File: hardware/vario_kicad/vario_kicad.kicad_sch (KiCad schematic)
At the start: 8 parts, among them U1 STM32L071CBTx, U2 BME280

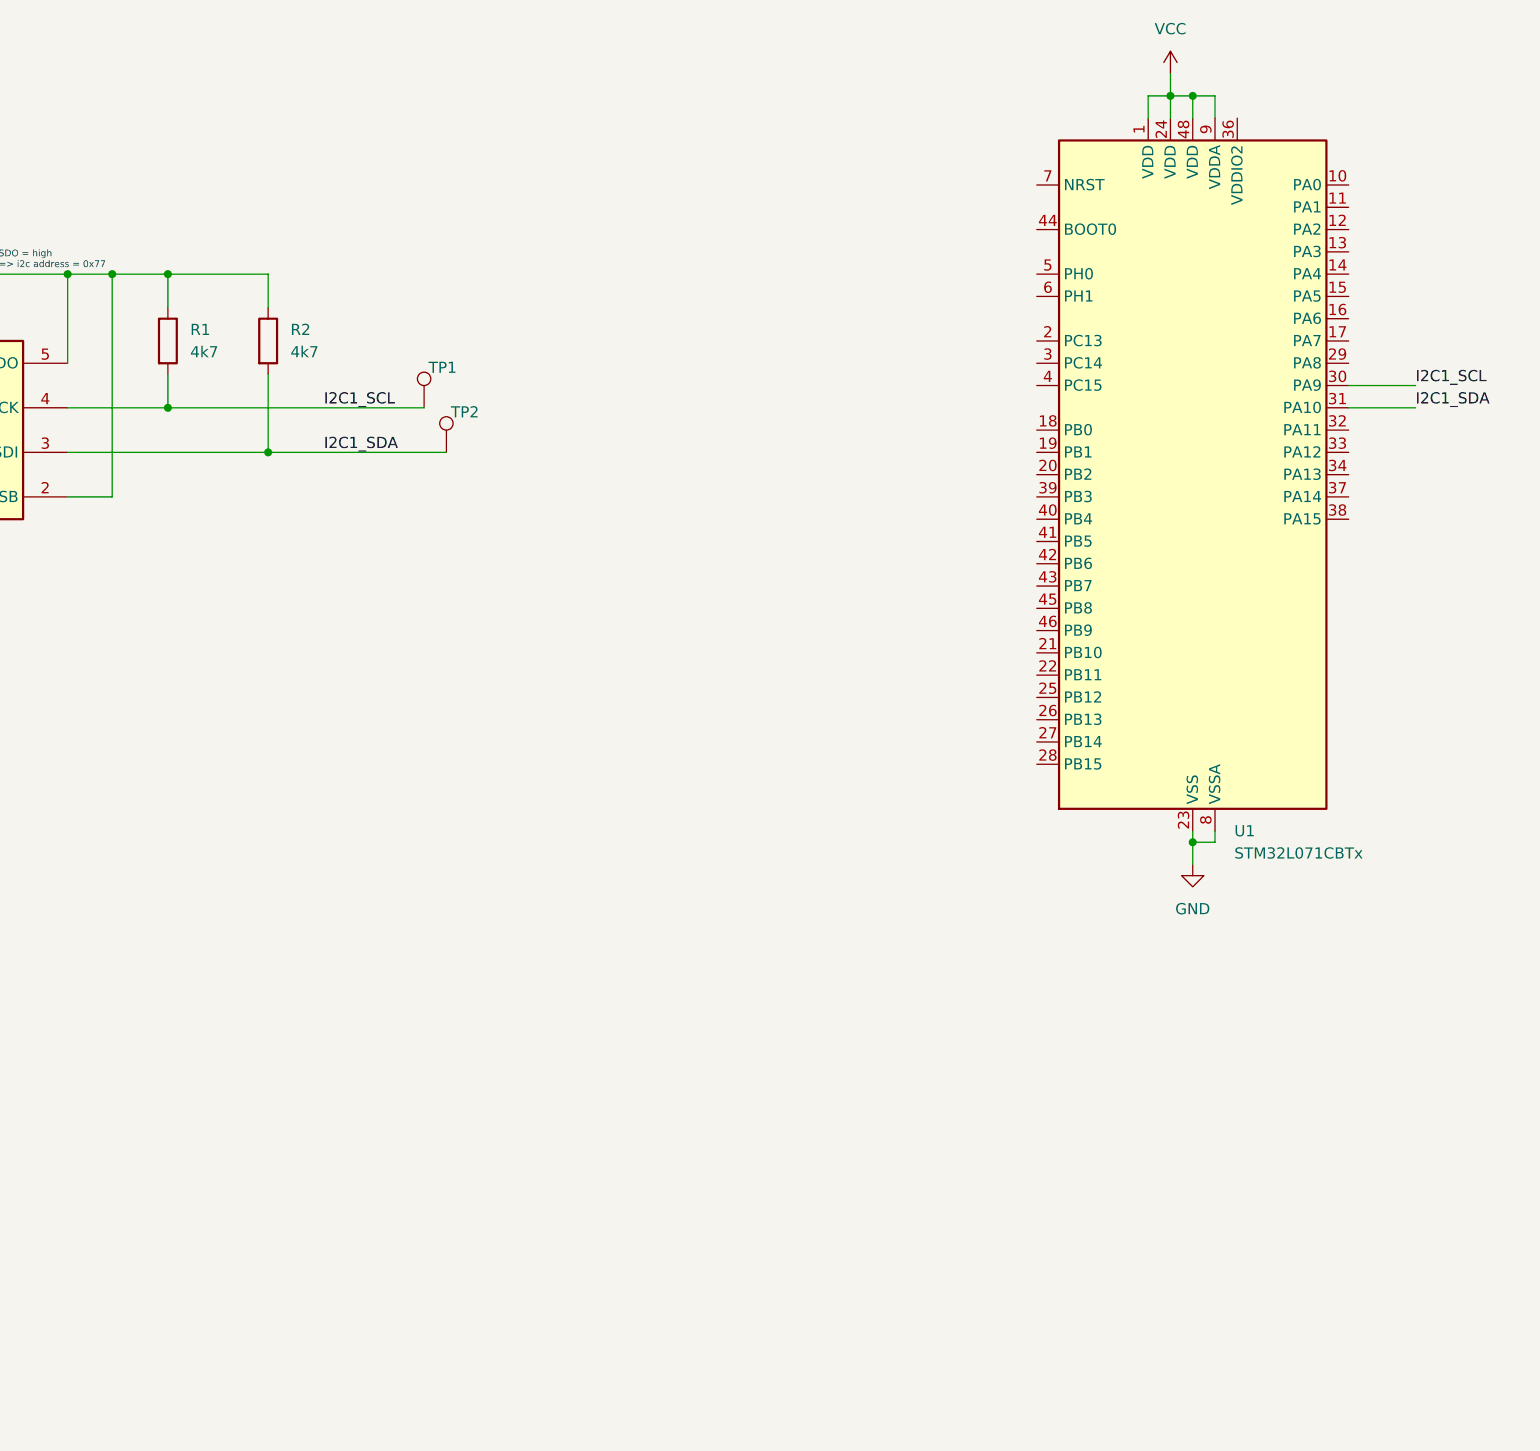
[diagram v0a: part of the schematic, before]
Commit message: add external memory chip
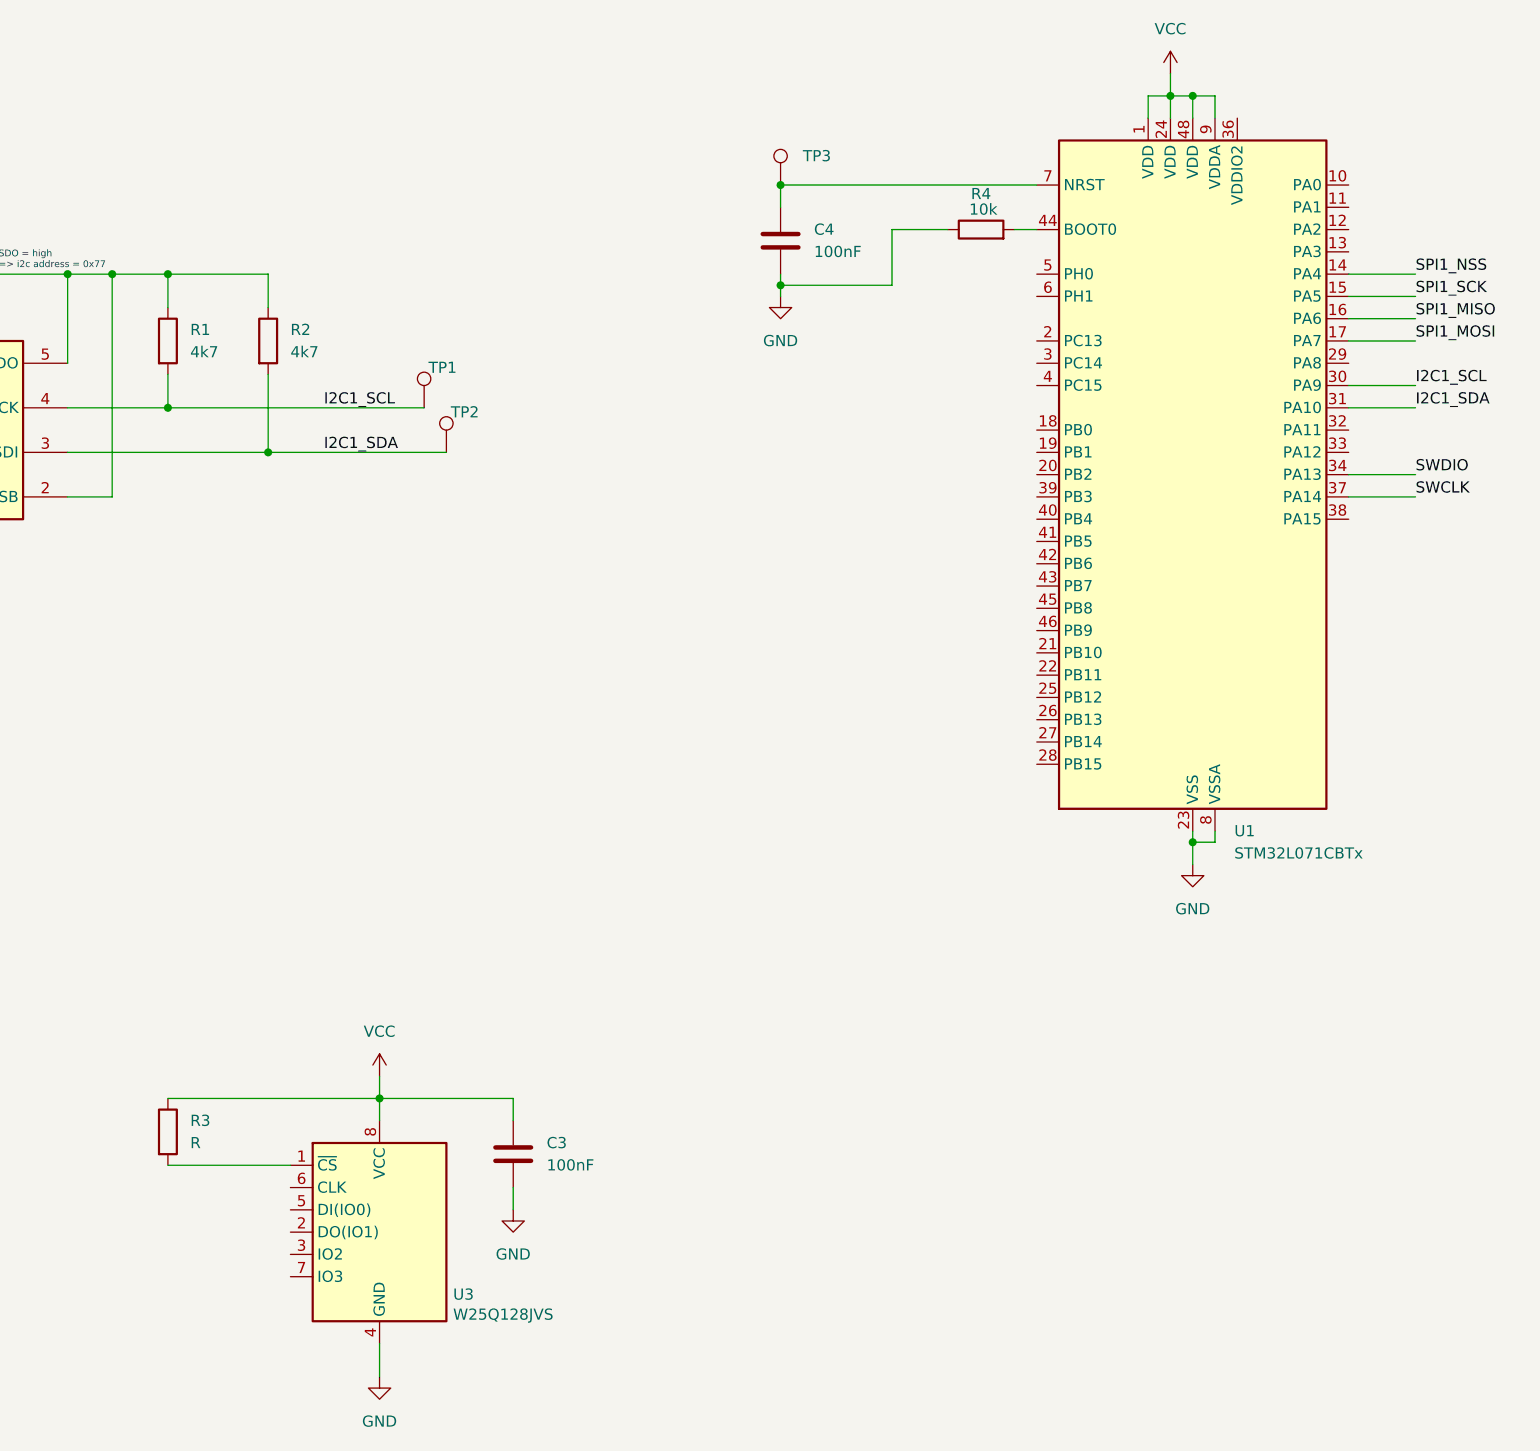
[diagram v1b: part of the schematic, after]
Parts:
- added C3, C4: 100nF, symbol Device:C
- added R3: R, symbol Device:R
- added R4: 10k, symbol Device:R
- added TP3: ~, symbol Connector:TestPoint
- added U3: W25Q128JVS, Package_SO:SOIC-8_5.23x5.23mm_P1.27mm, symbol Memory_Flash:W25Q128JVS
- TP1, TP2: value (none) -> ~
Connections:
- net GND: now also C3.2, C4.2, R4.1, U3.4 (GND)
- net VCC: now also C3.1, R3.1, U3.8 (VCC)
- net SPI1_NSS: now reaches U1.14 (PA4)
- net SPI1_SCK: now reaches U1.15 (PA5)
- net SPI1_MISO: now reaches U1.16 (PA6)
- net SPI1_MOSI: now reaches U1.17 (PA7)
- net SWDIO: now reaches U1.34 (PA13)
- net SWCLK: now reaches U1.37 (PA14)
- net at U1.44 (BOOT0): now also R4.2
- net at U1.7 (NRST): now also C4.1, TP3.1
- new net: R3.2, U3.1 (~{CS})

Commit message: update hw
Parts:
- added D1, D2, D3: LED, symbol Device:LED
- added R10, R11: 10k, symbol Device:R
- added R12, R13, R14: 330R, symbol Device:R
- added R5, R6, R7, R8, R9: 0R, symbol Device:R
- added TP4: ~, symbol Connector:TestPoint
- R3: value R -> 10k
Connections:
- net GND: now also R12.2, R13.2, R14.2
- net SPI1_MISO: now also R7.1
- net SPI1_MOSI: now also R6.1
- net SPI1_NSS: now also R8.1
- net SPI1_SCK: now also R5.1
- net VCC: now also R10.1, R11.1
- net BOOT0: now reaches R4.2, U1.44 (BOOT0)
- net BOOT0: now also TP4.1
- net NRST: now reaches C4.1, TP3.1, U1.7 (NRST)
- net at R3.2, U3.1 (~{CS}): now also R8.2, R9.2
- net at U3.2 (DO(IO1)): now also R7.2
- net MEM_WP: now reaches U3.3 (WP(IO2))
- net MEM_WP: now also R10.2
- net at U3.5 (DI(IO0)): now also R6.2
- net at U3.6 (CLK): now also R5.2
- net MEM_HOLD: now reaches U3.7 (IO3)
- net MEM_HOLD: now also R11.2
- net RED_LED: now reaches U1.10 (PA0)
- net RED_LED: now also D1.2 (A)
- net GREEN_LED: now reaches U1.11 (PA1)
- net GREEN_LED: now also D2.2 (A)
- net BLUE_LED: now reaches U1.12 (PA2)
- net BLUE_LED: now also D3.2 (A)
- new net: D2.1 (K), R13.1
- new net: D3.1 (K), R14.1
- new net: D1.1 (K), R12.1
- new net MEM_CS_ALT: R9.1
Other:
- moved on the sheet: C1, C2, C3, C4, R1, R2, R3, TP1, TP2, TP3, U2, U3

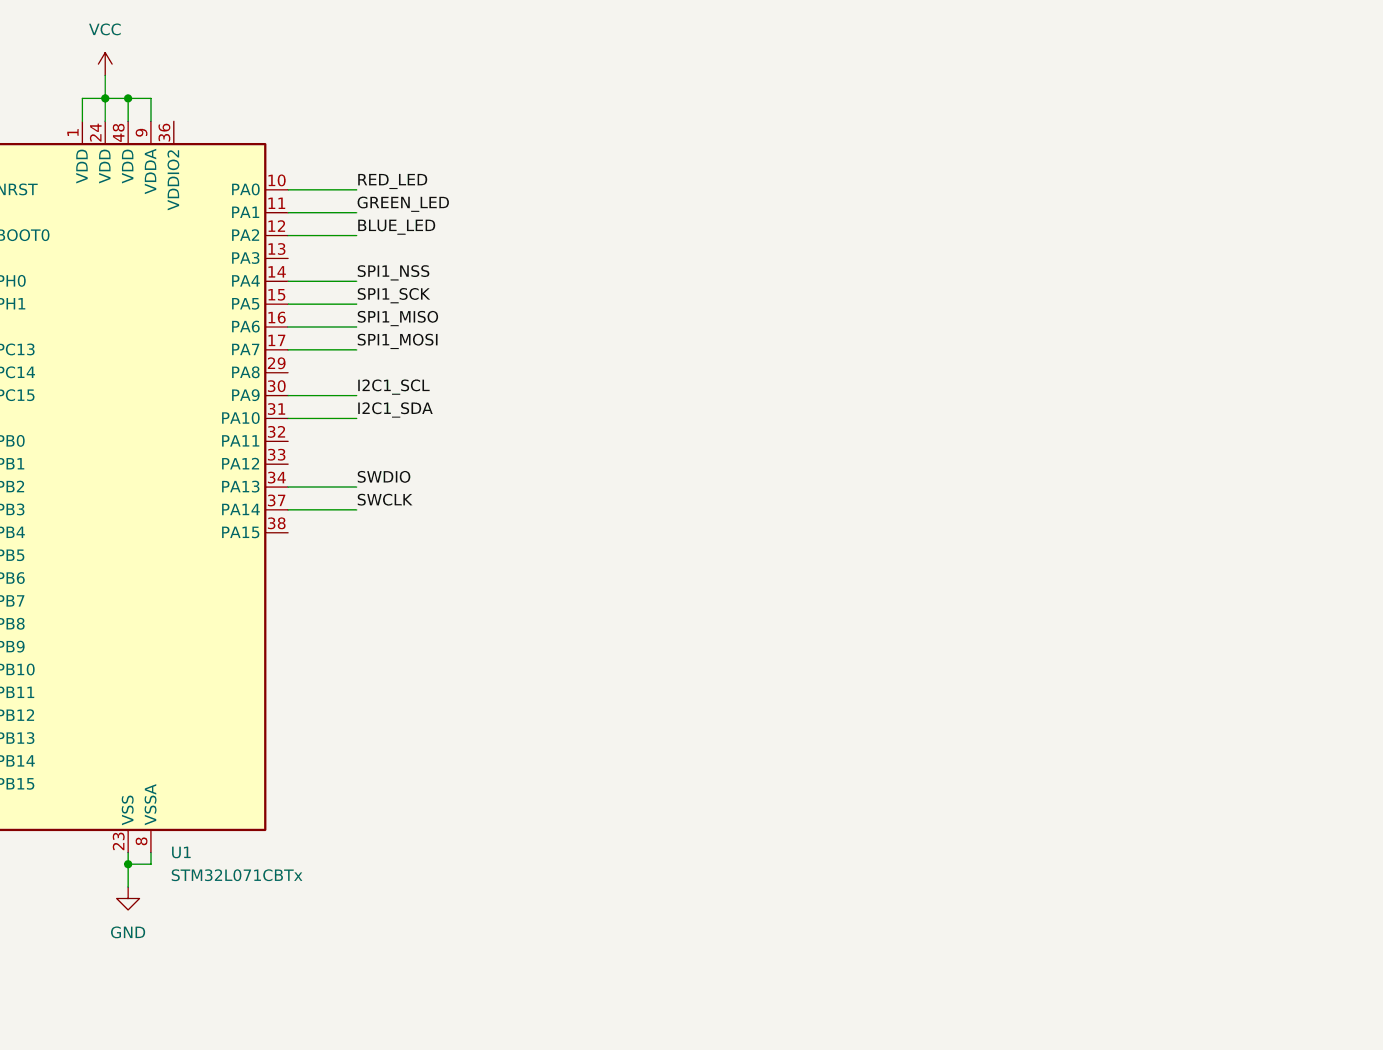
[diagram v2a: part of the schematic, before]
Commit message: update to stm32l072 processor for usb
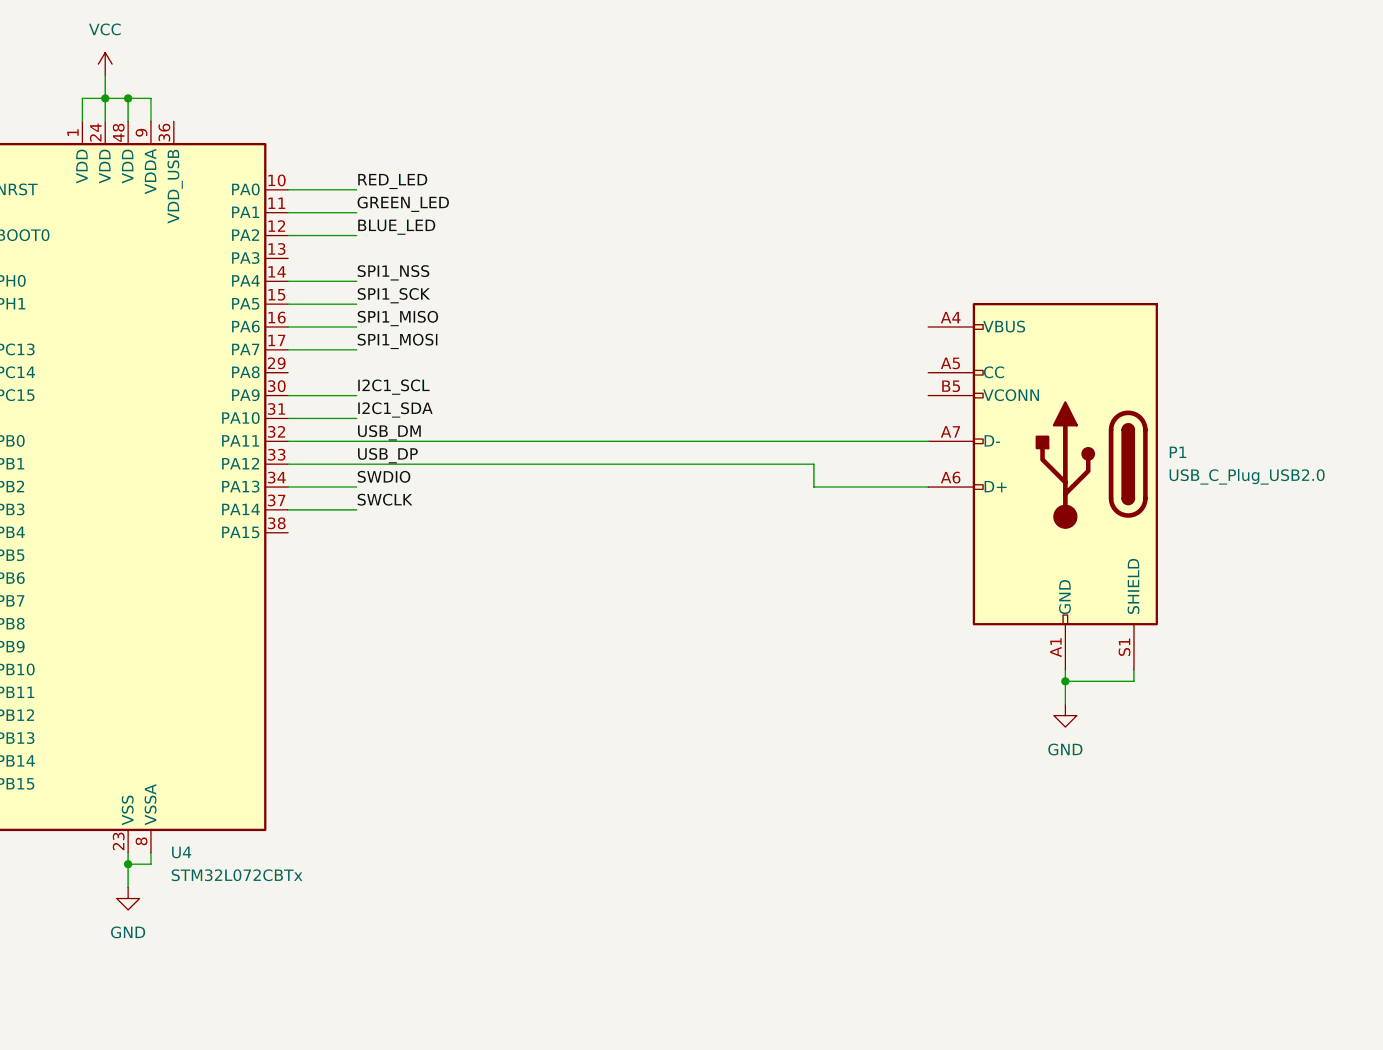
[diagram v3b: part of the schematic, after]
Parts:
- removed U1: STM32L071CBTx, Package_QFP:LQFP-48_7x7mm_P0.5mm, symbol MCU_ST_STM32L0:STM32L071CBTx
- added P1: USB_C_Plug_USB2.0, symbol Connector:USB_C_Plug_USB2.0
- added U4: STM32L072CBTx, Package_QFP:LQFP-48_7x7mm_P0.5mm, symbol MCU_ST_STM32L0:STM32L072CBTx
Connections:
- net BLUE_LED: now also U4.12 (PA2)
- net BOOT0: now also U4.44 (BOOT0)
- net GND: now also P1.A1 (GND), P1.A12 (GND), P1.B1 (GND), P1.B12 (GND), P1.S1 (SHIELD), U4.23 (VSS), U4.35 (VSS), U4.47 (VSS), U4.8 (VSSA)
- net GREEN_LED: now also U4.11 (PA1)
- net I2C1_SCL: now also U4.30 (PA9)
- net I2C1_SDA: now also U4.31 (PA10)
- net NRST: now also U4.7 (NRST)
- net RED_LED: now also U4.10 (PA0)
- net SPI1_MISO: now also U4.16 (PA6)
- net SPI1_MOSI: now also U4.17 (PA7)
- net SPI1_NSS: now also U4.14 (PA4)
- net SPI1_SCK: now also U4.15 (PA5)
- net SWCLK: now also U4.37 (PA14)
- net SWDIO: now also U4.34 (PA13)
- net VCC: now also U4.1 (VDD), U4.24 (VDD), U4.48 (VDD), U4.9 (VDDA)
- new net: P1.A4 (VBUS), P1.A9 (VBUS), P1.B4 (VBUS), P1.B9 (VBUS)
- new net USB_DM: P1.A7 (D-), U4.32 (PA11)
- new net USB_DP: P1.A6 (D+), U4.33 (PA12)

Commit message: afsd
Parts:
- added R15: 5k1, symbol Device:R
- added TP5, TP6: TestPoint, symbol Connector:TestPoint
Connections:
- net GND: now also R15.1
- net VBUS: now reaches P1.A4 (VBUS), P1.A9 (VBUS), P1.B4 (VBUS), P1.B9 (VBUS)
- net at P1.A5 (CC): now also R15.2
- net USB_DM renamed USB_D-
- net USB_D-: now also TP5.1
- net USB_DP renamed USB_D+
- net USB_D+: now also TP6.1
- no-connect marks 0 -> 2
